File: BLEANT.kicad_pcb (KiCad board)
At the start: 4 copper layers, 75.8 x 76.2 mm, 109 parts, among them IC1 FAN4010IL6X_F113, IC2 FAN4010IL6X_F113, J1 Conn_01x04_Male, J2 SC_19-20, J3 Conn_01x02, J4 Conn_01x02, J5 1909763-1, U1 nRF51x22-QFxx, U2 SN74LVC1T45DBVR, U3 MP5077GG-Z, U4 MP5077GG-Z, U5 MCP2515-xSO, U6 SN65HVD1050D, U7 SN74LVC1T45DBVR, X2 32.768kHz, Y1 16MHz

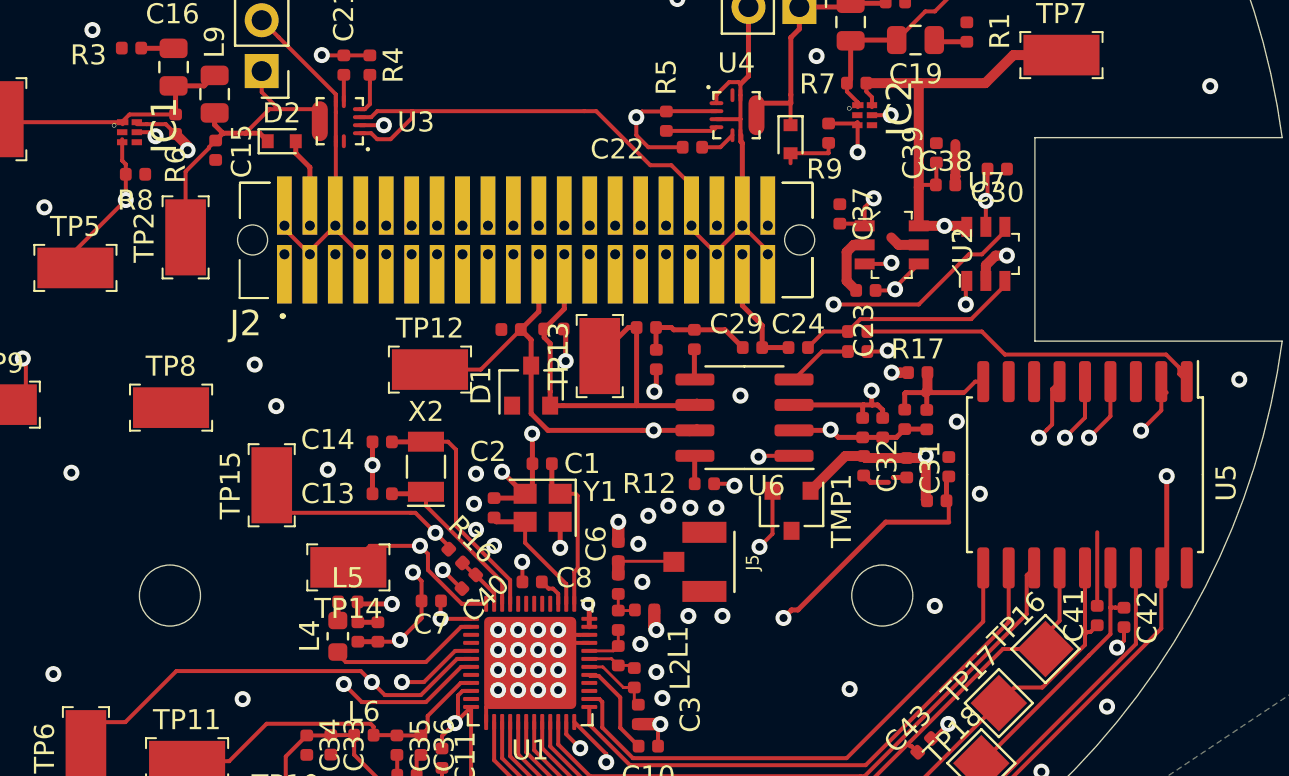
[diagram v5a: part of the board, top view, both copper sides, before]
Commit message: Fixed clearances
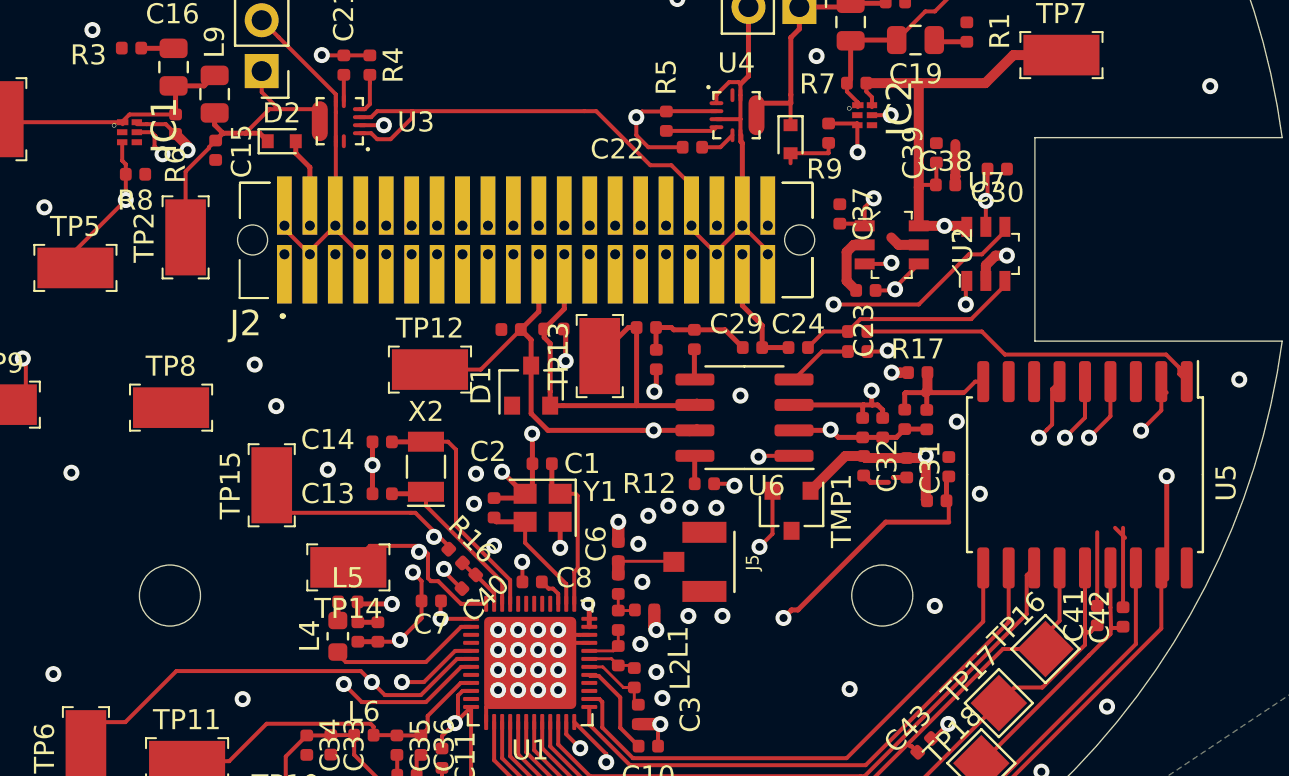
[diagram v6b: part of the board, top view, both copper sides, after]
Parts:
- moved C42 0.05 mm to (182.2, 145.8), turned to 90 degrees
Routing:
- net GND: track 94.5 -> 107.0 mm, vias 89 -> 87
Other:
- net class Default: clearance 0.15 -> 0.127; trace_width 0.25 -> 0.1
- rule trace_clearance: 0.15 -> 0.127
- rule trace_min: 0.1 -> 0
- rule via_min_size: 0.4 -> 0

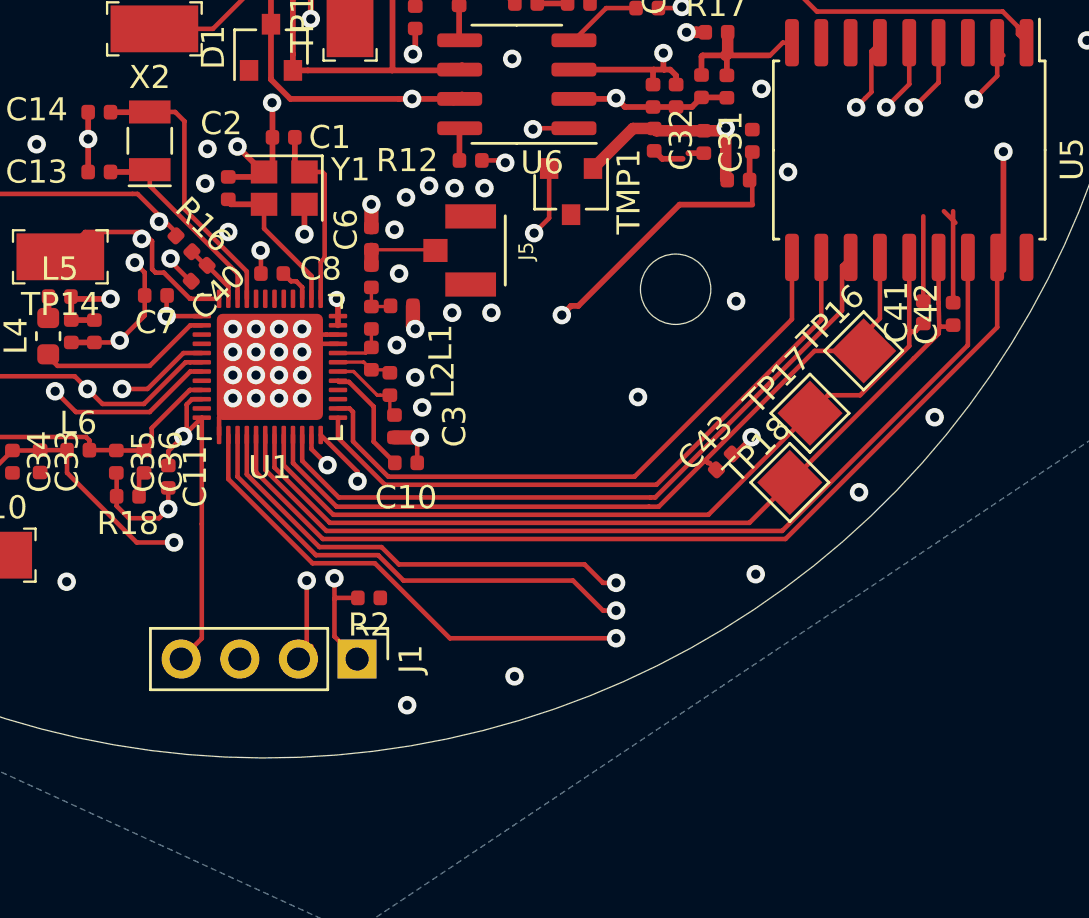
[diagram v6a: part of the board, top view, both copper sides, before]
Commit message: Fixed RF traces
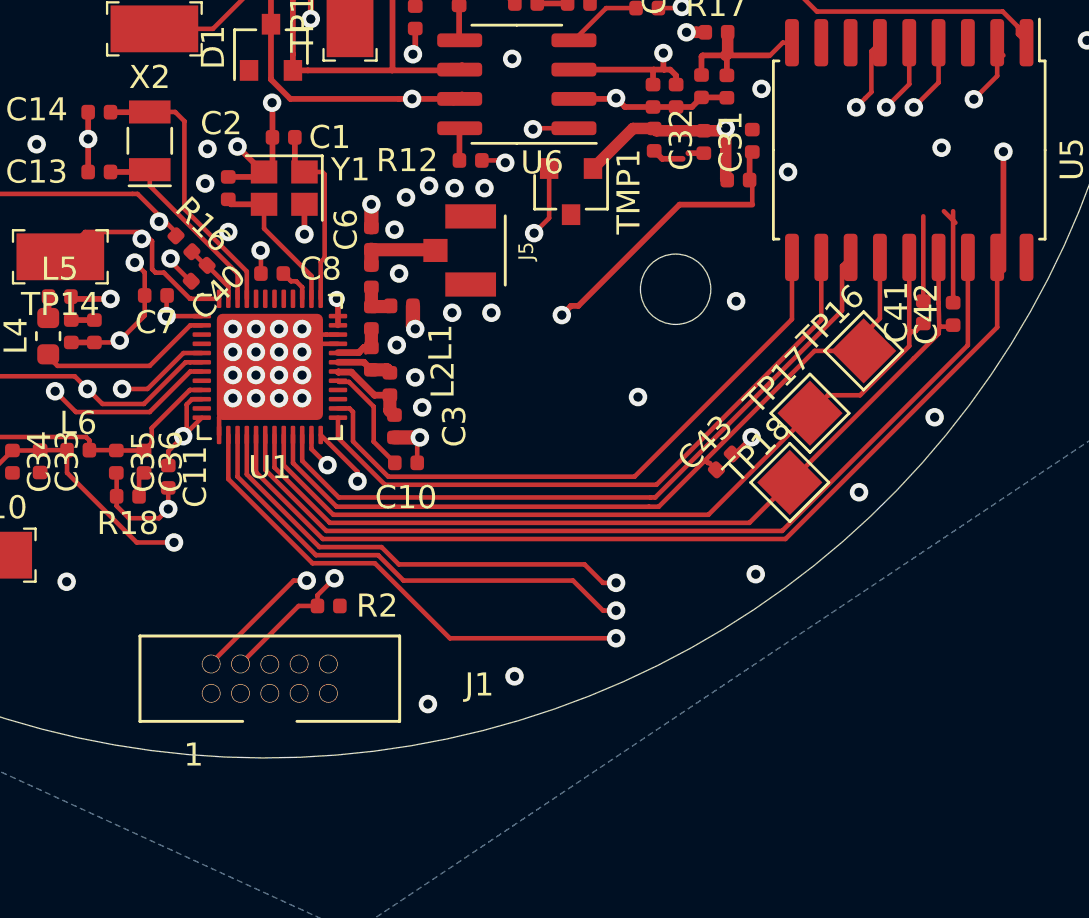
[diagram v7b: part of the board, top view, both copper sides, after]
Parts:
- J1: value Conn_01x04_Male -> SWD; footprint Connector_PinHeader_2.54mm:PinHeader_1x04_P2.54mm_Vertical -> BLE-ANT-Board:2X10_BOXHEADER
- moved J1 3.87 mm to (152.6, 161.7), turned to 0 degrees
- moved R2 1.78 mm to (155.2, 158.5)
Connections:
- J1 pad 1: SWDCLK -> +3V3
- J1 pad 4: +3V3 -> SWDCLK
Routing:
- net +3V3: track 31.6 -> 20.7 mm
- net SWDIO: track 11.3 -> 12.8 mm
- net SWDCLK: track 12.2 -> 13.2 mm
- net GND: vias 87 -> 88
